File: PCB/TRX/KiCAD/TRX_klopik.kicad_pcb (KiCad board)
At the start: 2 copper layers, 100 x 100 mm, 166 parts, among them J1 MIC, J10 Conn_01x01, J11 Conn_01x01, J12 BPF, J13 AF, J2 OUT, J3 13.6v, J4 RF, J5 Conn_01x05, J6 TX, J7 S-metr, J8 Conn_01x01, J9 Conn_01x01, K1 TQ2-12VDC, Q1 MMBT2222LT1G, Q10 BC847, Q11 BC847, Q12 BC847, Q2 BC857, Q3 BC857, Q4 BC857, Q5 BC847, Q6 BC847, Q7 BC847, Q8 2N7002, Q9 2N7002, T1 Transformer_1P_2S, T2 Transformer_1P_2S, T3 1_4, U1 ADE-1H+, U3 LM386, Y1 8.867Mhz, Y10 8.867Mhz, Y11 8.867Mhz, Y12 8.867Mhz, Y13 8.867Mhz, Y14 8.867Mhz, Y15 8.867Mhz, Y16 8.867Mhz, Y17 8.867Mhz, Y18 8.867Mhz, Y19 8.867Mhz, Y2 8.867Mhz, Y20 8.867Mhz, Y21 8.867Mhz, Y3 8.867Mhz, Y4 8.867Mhz, Y5 8.867Mhz, Y6 8.867Mhz, Y7 8.867Mhz, Y8 8.867Mhz, Y9 8.867Mhz

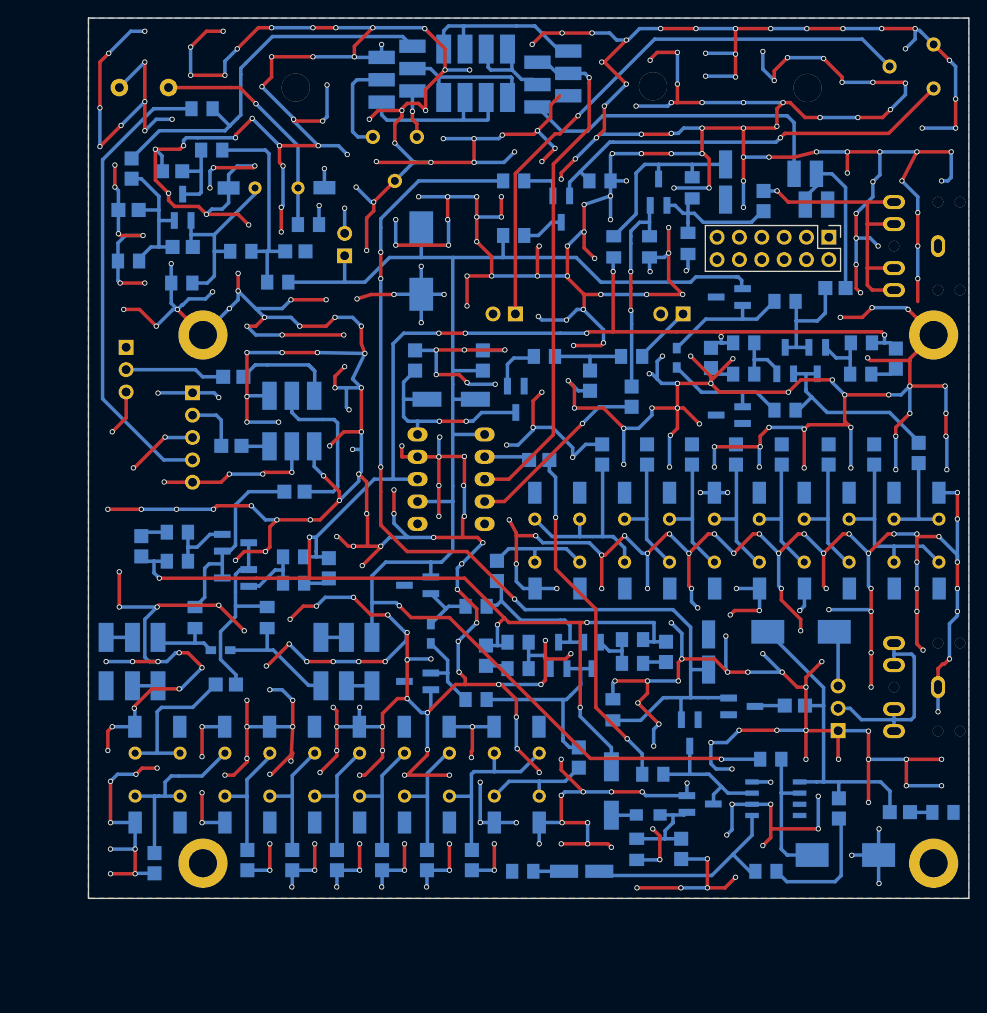
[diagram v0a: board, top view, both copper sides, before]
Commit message: add TRX PCB v1.15
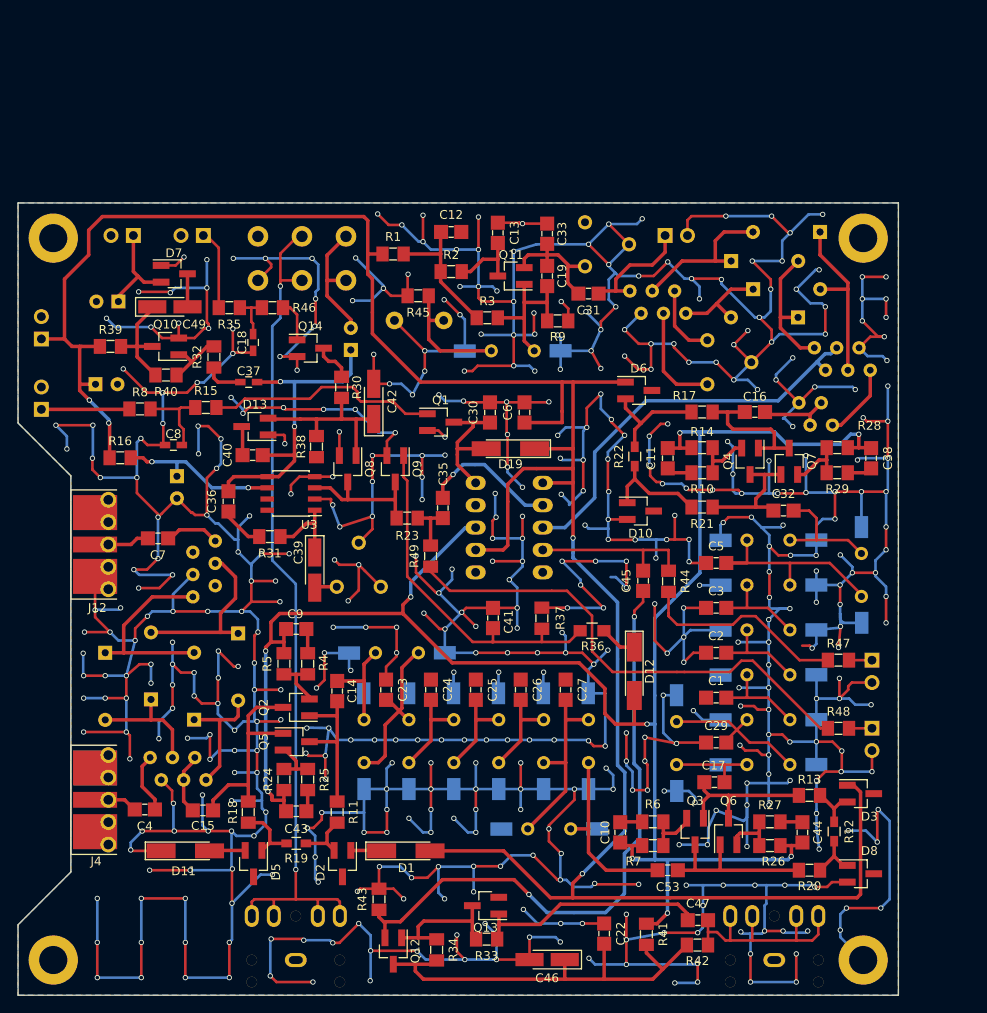
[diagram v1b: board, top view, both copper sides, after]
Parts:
- removed C21: 56, TRX_klopik:C_1206_0603
- removed C28: 62, TRX_klopik:C_1206_0603
- removed U1: ADE-1H+, TRX_klopik:CD636
- removed Y1, Y2, Y3, Y4: 8.867Mhz, TRX_klopik:Crystal_HC49-U_Vertical
- added C48: 47uF, Capacitors_ThroughHole:CP_Radial_D6.3mm_P2.50mm, B.Cu at (65.4, 53.2)
- added C49: 10uF, Capacitors_Tantalum_SMD:CP_Tantalum_Case-A_EIA-3216-18_Hand, F.Cu at (71.2, 53.8)
- added D18: D_Small, Diodes_ThroughHole:D_DO-35_SOD27_P7.62mm_Horizontal, B.Cu at (137.5, 51.8)
- added D19: LL4148, Diodes_SMD:D_MiniMELF_Handsoldering, F.Cu at (109.9, 69.9)
- added D20: D_Small, Diodes_ThroughHole:D_DO-35_SOD27_P7.62mm_Horizontal, B.Cu at (145.1, 45.3)
- added J14: BFO, Pin_Headers:Pin_Header_Straight_1x02_Pitch2.54mm, B.Cu at (127.5, 45.7)
- added J15: AGC, Pin_Headers:Pin_Header_Straight_1x02_Pitch2.54mm, B.Cu at (75.0, 45.7)
- added Q13: BC847, TO_SOT_Packages_SMD:SOT-23_Handsoldering, F.Cu at (107.1, 121.8)
- added Q14: BC847, TO_SOT_Packages_SMD:SOT-23_Handsoldering, F.Cu at (87.2, 58.5)
- added R46: 1k, TRX_klopik:R_1206_0603, F.Cu at (82.9, 53.9)
- added R47: 0R, TRX_klopik:R_1206_0603, F.Cu at (147.2, 93.9)
- added R48: 0R, TRX_klopik:R_1206_0603, F.Cu at (147.2, 101.7)
- added R49: 0R, TRX_klopik:R_1206_0603, F.Cu at (100.9, 82.1)
- added RV3: 200R, Potentiometers:Potentiometer_Trimmer_Piher_PT-6v_Horizontal, B.Cu at (90.2, 85.6)
- added RV4: POT_Dual, TRX_klopik:Potentiometer_WH148_Double, B.Cu at (81.2, 45.8)
- added T4: Transformer_1P_2S, TRX_klopik:HF_transf3, B.Cu at (69.0, 105.0)
- added T5: Transformer_1P_2S, TRX_klopik:HF_transf3, B.Cu at (76.4, 80.4)
- C1, C10, C11, C12, C13, C14, C15, C16, C17, C19, C2, C23, C24, C25, C26, C27, C29, C3, C30, C31, C32, C33, C35, C36, C38, C4, C40, C41, C42, C43, C44, C45, C46, C5, C53, C7, C9, D1, D10, D11, D12, D13, D3, D6, D8, Q10, Q11, Q12, Q2, Q3, Q4, Q5, Q6, Q7, Q8, Q9, R1, R10, R11, R12, R13, R14, R16, R17, R18, R19, R2, R20, R21, R22, R23, R24, R25, R26, R27, R28, R29, R3, R30, R31, R36, R37, R38, R4, R45, R5, R6, R7, R8, R9, U3: moved to F.Cu
- C18, C37: value 100nF -> 10nF; footprint TRX_klopik:C_1206_0603 -> Capacitors_SMD:C_0603_HandSoldering; moved to F.Cu
- C20, C34, C57: footprint Capacitors_Tantalum_SMD:CP_Tantalum_Case-D_EIA-7343-31_Hand -> Capacitors_ThroughHole:CP_Radial_D6.3mm_P2.50mm
- C22: value 62 -> 100nF; moved to F.Cu
- C39: value 10uF -> 22uF; moved to F.Cu
- C47: value 100nF -> 330nF; moved to F.Cu
- C6: value 56 -> 100nF; moved to F.Cu
- C8: value 15nF -> 10nF; footprint TRX_klopik:C_1206_0603 -> Capacitors_SMD:C_0603_HandSoldering; moved to F.Cu
- D14, D15, D16, D17, D4, D9: value LL4148 -> D_Small; footprint Diodes_SMD:D_MiniMELF_Handsoldering -> Diodes_ThroughHole:D_DO-35_SOD27_P7.62mm_Horizontal
- D2, D5, D7: value LL4148 -> BAV99; footprint Diodes_SMD:D_MiniMELF_Handsoldering -> TO_SOT_Packages_SMD:SOT-23_Handsoldering; moved to F.Cu
- J12: value BPF -> VFO; footprint Pin_Headers:Pin_Header_Straight_2x06_Pitch2.54mm -> TRX_klopik:RFCONNECTOR
- J13: value AF -> VOX; footprint Pin_Headers:Pin_Header_Straight_1x03_Pitch2.54mm -> Pin_Headers:Pin_Header_Straight_1x02_Pitch2.54mm
- J4: value RF -> BPF; footprint Pin_Headers:Pin_Header_Angled_1x03_Pitch2.54mm -> TRX_klopik:RFCONNECTOR; moved to F.Cu
- J5: value Conn_01x05 -> AUDIO IN; footprint Pin_Headers:Pin_Header_Straight_1x05_Pitch2.54mm -> Pin_Headers:Pin_Header_Straight_1x02_Pitch2.54mm
- Q1: value MMBT2222LT1G -> BC847; moved to F.Cu
- R15: value 680 -> 1k; moved to F.Cu
- R32: value 10 -> 100k; moved to F.Cu
- R33: value 100R -> 300k; moved to F.Cu
- R34: value 20k -> 6.2k; moved to F.Cu
- R35: value 100 -> 1k; moved to F.Cu
- R39: value 150k -> 2.4k; moved to F.Cu
- R40: value 8k2 -> 330k; moved to F.Cu
- R41: value 15k -> 330R; moved to F.Cu
- R42: value 1k -> 4.7k; moved to F.Cu
- R43: value 470R -> 680R; moved to F.Cu
- R44: value 0 -> 0R; moved to F.Cu
- RV2: value 100 -> 1k
- T1: footprint HF12_2 -> TRX_klopik:HF_transf3
- T2: footprint HF12 -> TRX_klopik:HF_transf3
- T3: footprint 1_4 -> TRX_klopik:TF14
- moved R32 97.6 mm to (76.2, 59.5), turned to 90 degrees
- moved Q12 91.3 mm to (96.6, 127.0), turned to 270 degrees
- moved R34 91.3 mm to (101.5, 126.8), turned to 90 degrees
- moved C46 90.6 mm to (114.1, 128.0), turned to 180 degrees
- moved C37 88.6 mm to (80.2, 62.4), turned to 0 degrees
- moved J12 87.9 mm to (65.4, 80.8), turned to 0 degrees
- moved R42 87.5 mm to (131.2, 126.3)
- moved C20 87.3 mm to (72.0, 73.0), turned to 270 degrees
- moved J5 86.1 mm to (151.0, 101.7)
- moved J1 83.2 mm to (139.9, 128.0), turned to 0 degrees
- moved C47 82.0 mm to (131.2, 123.5), turned to 0 degrees
- moved D17 81.6 mm to (74.0, 100.7), turned to 90 degrees
- moved R16 81.4 mm to (65.6, 71.0)
- moved R43 80.2 mm to (95.0, 121.1), turned to 90 degrees
- moved R33 80.0 mm to (107.2, 125.6), turned to 0 degrees
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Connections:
- C18 pad 1: 13.6V -> GND
- C18 pad 2: GND -> Net-(C18-Pad2)
- C46 pad 1: Net-(C46-Pad1) -> Net-(C22-Pad2)
- C6 pad 1: GND -> 13.6V
- C6 pad 2: Net-(C6-Pad2) -> GND
- C7 pad 2: VFO -> Net-(C7-Pad2)
- D15 pad 1: 13.6V -> Net-(D15-Pad1)
- D15 pad 2: RELAY -> Net-(D15-Pad2)
- D17 pad 1: Net-(D16-Pad2) -> Net-(D15-Pad2)
- D17 pad 2: Net-(D14-Pad1) -> Net-(D16-Pad1)
- D2 pad 1: Net-(D2-Pad1) -> Net-(D1-Pad1)
- D2 pad 2: Net-(D1-Pad1) -> Net-(D2-Pad2)
- D4 pad 2: Net-(D16-Pad1) -> Net-(D18-Pad1)
- D5 pad 2: Net-(D2-Pad1) -> Net-(D11-Pad2)
- D7 pad 1: Net-(D7-Pad1) -> GND
- D7 pad 2: Net-(D7-Pad2) -> Net-(C48-Pad1)
- D9 pad 1: Net-(D11-Pad2) -> Net-(D16-Pad2)
- D9 pad 2: Net-(D7-Pad1) -> Net-(D15-Pad1)
- J12 pad 1: (no net) -> Net-(C7-Pad2)
- J12 pad 2: (no net) -> GND
- J13 pad 1: GND -> Net-(J13-Pad1)
- J13 pad 2: Net-(J13-Pad2) -> GND
- J2 pad 2: Net-(J13-Pad2) -> Net-(J2-Pad2)
- J2 pad 3: Net-(J13-Pad2) -> Net-(J2-Pad2)
- J2 pad 4: Net-(J13-Pad2) -> Net-(J2-Pad2)
- J2 pad 5: Net-(J13-Pad2) -> Net-(J2-Pad2)
- J4 pad 1: GND -> Net-(C4-Pad2)
- J4 pad 2: Net-(C4-Pad2) -> GND
- J5 pad 1: GND -> Net-(J5-Pad1)
- J5 pad 2: VFO -> GND
- J7 pad 1: Net-(J7-Pad1) -> Net-(C48-Pad1)
- Q10 pad 2: Net-(Q10-Pad2) -> GND
- Q10 pad 3: Net-(Q10-Pad3) -> Net-(C49-Pad1)
- Q12 pad 1: Net-(C47-Pad1) -> Net-(Q12-Pad1)
- Q12 pad 3: Net-(C46-Pad1) -> Net-(C22-Pad2)
- R11 pad 1: Net-(D5-Pad1) -> Net-(D2-Pad2)
- R15 pad 1: Net-(C19-Pad1) -> Net-(C8-Pad2)
- R15 pad 2: GND -> Net-(Q1-Pad1)
- R18 pad 2: Net-(D7-Pad2) -> Net-(D5-Pad1)
- R19 pad 1: Net-(D5-Pad1) -> Net-(D2-Pad2)
- R19 pad 2: Net-(D7-Pad2) -> Net-(D5-Pad1)
- R30 pad 1: Net-(C8-Pad2) -> Net-(C42-Pad1)
- R30 pad 2: Net-(J6-Pad1) -> Net-(Q14-Pad3)
- R32 pad 2: GND -> Net-(Q10-Pad1)
- R33 pad 1: Net-(C46-Pad1) -> Net-(Q12-Pad1)
- R33 pad 2: TX -> Net-(C47-Pad1)
- R34 pad 1: Net-(C46-Pad1) -> Net-(C22-Pad2)
- R34 pad 2: Net-(C47-Pad1) -> Net-(Q12-Pad1)
- R35 pad 1: Net-(C39-Pad2) -> Net-(C18-Pad2)
- R35 pad 2: GND -> Net-(J15-Pad1)
- R39 pad 1: Net-(C42-Pad1) -> 13.6V
- R39 pad 2: Net-(Q10-Pad1) -> Net-(C49-Pad1)
- R40 pad 1: 13.6V -> Net-(Q10-Pad1)
- R40 pad 2: Net-(Q10-Pad3) -> Net-(C49-Pad1)
- R41 pad 1: Net-(C47-Pad1) -> Net-(C22-Pad2)
- R41 pad 2: GND -> TX
- R42 pad 1: Net-(Q10-Pad2) -> Net-(C22-Pad2)
- R42 pad 2: GND -> Net-(C47-Pad2)
- R44 pad 1: BFO -> Net-(C45-Pad2)
- R44 pad 2: Net-(C31-Pad1) -> Net-(R44-Pad2)
- R8 pad 1: Net-(Q1-Pad1) -> Net-(J6-Pad1)
- RV2 pad 1: Net-(Q10-Pad2) -> GND
- RV2 pad 2: Net-(J7-Pad1) -> GND
- RV2 pad 3: GND -> Net-(C19-Pad1)
- T1 pad 3: Net-(D16-Pad2) -> Net-(D18-Pad2)
- T2 pad 6: Net-(D16-Pad1) -> Net-(D18-Pad1)
- Y11 pad 2: Net-(C28-Pad2) -> Net-(C53-Pad2)
- Y12 pad 1: Net-(C28-Pad2) -> Net-(C27-Pad2)
- Y13 pad 2: Net-(C21-Pad2) -> Net-(C29-Pad2)
- Y14 pad 1: Net-(C21-Pad2) -> Net-(C17-Pad2)
- Y20 pad 2: Net-(C6-Pad2) -> Net-(C32-Pad2)
- Y21 pad 1: Net-(C6-Pad2) -> Net-(C5-Pad2)
- Y5 pad 2: Net-(C22-Pad2) -> Net-(C23-Pad2)
- Y6 pad 1: Net-(C22-Pad2) -> Net-(C14-Pad2)
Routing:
- net GND: track 1931.8 -> 1795.5 mm, vias 509 -> 490
- net Net-(J2-Pad2): track 0.00 -> 97.8 mm, vias 0 -> 2
- net 13.6V: track 181.5 -> 278.4 mm, vias 2 -> 4
- net Net-(C42-Pad1): track 117.3 -> 20.5 mm, vias 4 -> 0
- net Net-(J7-Pad1): track 66.1 -> 0.00 mm, vias 1 -> 0
- net Net-(R48-Pad1): track 0.00 -> 56.5 mm
- net BFO: track 52.7 -> 0.00 mm
- net Net-(Q10-Pad2): track 48.9 -> 0.00 mm, vias 1 -> 0
- net Net-(C45-Pad1): track 23.8 -> 71.0 mm
- net Net-(C35-Pad2): track 40.1 -> 5.97 mm, vias 2 -> 0
- net Net-(C31-Pad1): track 44.0 -> 13.8 mm
- net Net-(C41-Pad2): track 11.3 -> 40.4 mm
- net Net-(T1-Pad1): track 37.1 -> 8.57 mm
- net Net-(C22-Pad2): track 21.3 -> 48.5 mm
- net Net-(R44-Pad2): track 0.00 -> 23.7 mm
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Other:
- board size 100 x 100 mm -> 100 x 90 mm
- net class Default: trace_width 0.4 -> 0.3
- board text added: "+13.6v"
- board text added: "AGC"
- board text added: "KLOPIK v1.15 TRX"
- board text removed: "+13.8V"
- board text removed: "BFO"
- board text removed: "VFO"

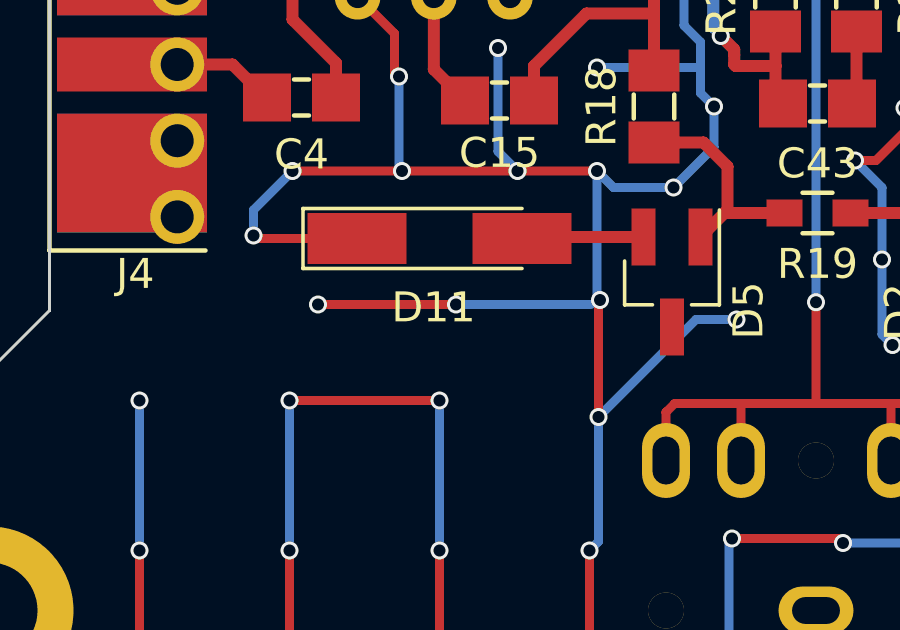
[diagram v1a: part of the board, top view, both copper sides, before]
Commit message: add BPF PCB
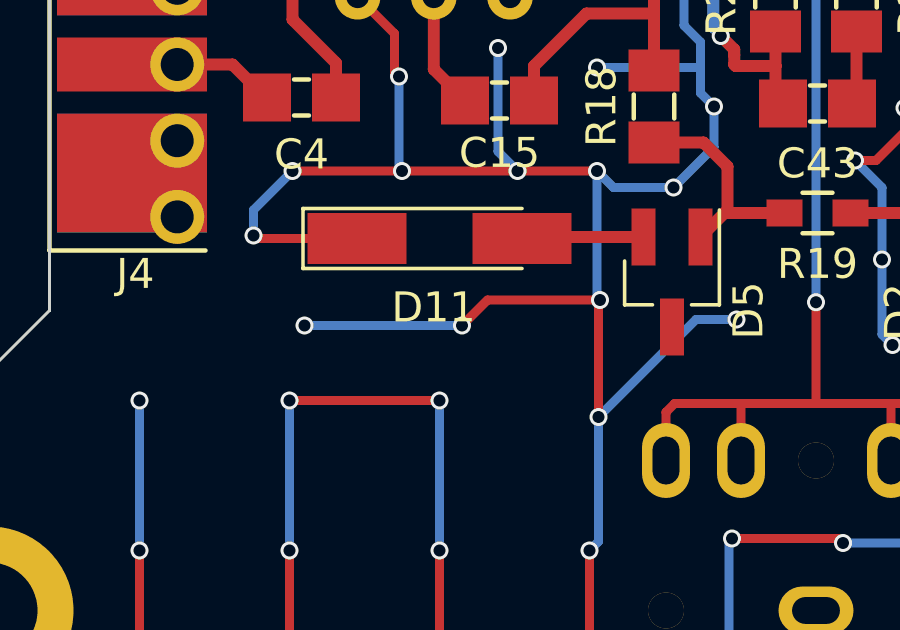
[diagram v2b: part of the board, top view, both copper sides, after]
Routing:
- net GND: track 1795.5 -> 1805.7 mm, vias 490 -> 492
- net (no net): track 9.10 -> 0.00 mm, vias 2 -> 0
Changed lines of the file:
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@@
     (thickness 1.6)
     (drawings 13)
-    (tracks 2222)
+    (tracks 2223)
     (zones 0)
     (modules 176)
@@
       (drillshape 0)
       (scaleselection 1)
-      (outputdirectory gerber_files/))
+      (outputdirectory gerber/))
   )
   (net 0 "")
@@
   (gr_line (start 54 132) (end 154 132) (angle 90) (layer Edge.Cuts) (width 0.1))
   (gr_line (start 54 124) (end 54 132) (angle 90) (layer Edge.Cuts) (width 0.1))
-  (segment (start 78.05 117.8) (end 73.55 117.8) (width 0.3) (layer B.Cu) (net 0))
-  (via (at 68.95 117.8) (size 0.6) (drill 0.4) (layers F.Cu B.Cu) (net 0))
-  (segment (start 73.55 117.8) (end 68.95 117.8) (width 0.3) (layer F.Cu) (net 0))
-  (via (at 73.55 117.8) (size 0.6) (drill 0.4) (layers F.Cu B.Cu) (net 0))
+  (segment (start 78.35 117.65) (end 74.6 117.65) (width 0.3) (layer F.Cu) (net 1))
+  (via (at 68.5 118.5) (size 0.6) (drill 0.4) (layers F.Cu B.Cu) (net 1))
+  (segment (start 73.75 118.5) (end 68.5 118.5) (width 0.3) (layer B.Cu) (net 1))
+  (via (at 73.75 118.5) (size 0.6) (drill 0.4) (layers F.Cu B.Cu) (net 1))
+  (segment (start 74.6 117.65) (end 73.75 118.5) (width 0.3) (layer F.Cu) (net 1))
   (segment (start 78.3 121.55) (end 78.3 125.7) (width 0.3) (layer B.Cu) (net 1))
   (via (at 63 121) (size 0.6) (drill 0.4) (layers F.Cu B.Cu) (net 1))
@@
   (segment (start 85.7 54.7) (end 85.7 57.55) (width 0.3) (layer F.Cu) (net 92))
   (segment (start 84.9 53.9) (end 85.7 54.7) (width 0.3) (layer F.Cu) (net 92))
-  (segment (start 80.7 56.9) (end 80.7 55.7) (width 0.3) (layer F.Cu) (net 93) (status 400000))
+  (segment (start 80.7 56.9) (end 80.7 55.7) (width 0.3) (layer F.Cu) (net 93))
   (segment (start 80.7 55.7) (end 80.5 55.5) (width 0.3) (layer F.Cu) (net 93))
   (segment (start 80.5 53.9) (end 80.5 55.5) (width 0.3) (layer F.Cu) (net 93))
